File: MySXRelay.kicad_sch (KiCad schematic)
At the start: 52 parts, among them K1 FH44L-1AT-L1-DC5V, U1 MIC4427, U2 BL0942, U3 BP2525X, U4 Si8642BB-B-IS1, U5 MCP1703Ax-180xxTT, U8 AP2204K-ADJ, U9 ST485E

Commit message: update pcb (WIP)
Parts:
- removed C2: 1u, Capacitor_SMD:C_0603_1608Metric, symbol Device:C
- removed C3: 22u, Capacitor_SMD:C_1206_3216Metric, symbol Device:C
- removed D1, D2: BAT54S, Package_TO_SOT_SMD:SOT-23, symbol Diode:BAT54S
- removed K1: FH44L-1AT-L1-DC5V, MySXRelay:RELAY-TH_FH44L-1AT-L1-DC5V, symbol MySXRelay:Relay_SPST_Latching_1coil
- removed R1: 10k, Resistor_SMD:R_0603_1608Metric, symbol Device:R
- removed R21: 9.1k, Resistor_SMD:R_0603_1608Metric, symbol Device:R
- removed R23: 3k, Resistor_SMD:R_0603_1608Metric, symbol Device:R
- removed U1: MIC4427, Package_SO:SOIC-8_3.9x4.9mm_P1.27mm, symbol Driver_FET:MIC4427
- added J3: Relay, MySXRelay:edge_connector, symbol MySXRelay:edge_connector
- C1: value 100n -> 10u; footprint Capacitor_SMD:C_0402_1005Metric -> Capacitor_SMD:C_0603_1608Metric
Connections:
- net +5V: now also J3.4 (VCC); no longer C1.1
- net D5: now also J3.3 (REL)
- net GND: now also J3.5 (GND); no longer C1.2
- net GND1: now also C1.1
- net L_IN: now also J3.1 (A1)
- net L_OUT: now also J3.2 (A2)
- net at U8.4 (ADJ): now also C1.2
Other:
- moved on the sheet: C19

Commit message: update pcb (WIP)
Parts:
- C1: value 10u -> 100p; footprint Capacitor_SMD:C_0603_1608Metric -> Capacitor_SMD:C_0402_1005Metric
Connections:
- net BP2525_DRAIN: now reaches C5.1, D5.1 (K), U3.4 (DRAIN)
- net BP2525_CS: now reaches R7.2, U3.5 (CS)
- net L_SENSE: now reaches R17.1, R18.2
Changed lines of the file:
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@@
 	)
 	(junction
+		(at 162.56 67.31)
+		(diameter 0)
+		(color 0 0 0 0)
+	)
+	(junction
 		(at 96.52 119.38)
 		(diameter 0)
@@
 	(wire
 		(pts
+			(xy 166.37 63.5) (xy 162.56 63.5)
+		)
+		(stroke
+			(width 0)
+			(type default)
+		)
+	)
+	(wire
+		(pts
 			(xy 223.52 106.68) (xy 226.06 106.68)
 		)
@@
 	(wire
 		(pts
+			(xy 162.56 63.5) (xy 162.56 67.31)
+		)
+		(stroke
+			(width 0)
+			(type default)
+		)
+	)
+	(wire
+		(pts
 			(xy 87.63 160.02) (xy 68.58 160.02)
 		)
@@
 		)
 	)
+	(label "BP2525_CS"
+		(at 175.26 143.51 90)
+		(fields_autoplaced yes)
+		(effects
+			(font
+				(size 1.27 1.27)
+			)
+			(justify left bottom)
+		)
+	)
+	(label "BP2525_DRAIN"
+		(at 173.99 119.38 0)
+		(fields_autoplaced yes)
+		(effects
+			(font
+				(size 1.27 1.27)
+			)
+			(justify left bottom)
+		)
+	)
+	(global_label "L_SENSE"
+		(shape input)
+		(at 166.37 63.5 0)
+		(fields_autoplaced yes)
+		(effects
+			(font
+				(size 1.27 1.27)
+			)
+			(justify left)
+		)
+		(property "Intersheetrefs" "${INTERSHEET_REFS}"
+			(at 177.3984 63.5 0)
+			(effects
+				(font
+					(size 1.27 1.27)
+				)
+				(justify left)
+				(hide yes)
+			)
+		)
+	)
 	(global_label "RS485_TX"
 		(shape input)
@@
 		)
 		(property "Netclass" "Mains_HV"
-			(at 188.976 116.332 0)
+			(at 188.976 115.824 0)
 			(effects
 				(font
@@
 		(on_board yes)
 		(dnp no)
-		(fields_autoplaced yes)
 		(property "Reference" "#PWR032"
 			(at 162.56 64.77 0)
@@
 		)
 		(property "Value" "GND"
-			(at 162.56 63.5 0)
+			(at 159.258 60.706 0)
 			(effects
 				(font
@@
 			)
 		)
-		(property "Value" "10u"
+		(property "Value" "100p"
 			(at 92.71 114.3001 0)
 			(effects
@@
 			)
 		)
-		(property "Footprint" "Capacitor_SMD:C_0603_1608Metric"
+		(property "Footprint" "Capacitor_SMD:C_0402_1005Metric"
 			(at 95.5548 111.76 0)
 			(effects

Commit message: relay module updated
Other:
- moved on the sheet: J3
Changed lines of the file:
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@@
 	(wire
 		(pts
-			(xy 62.23 46.99) (xy 63.5 46.99)
+			(xy 44.45 55.88) (xy 45.72 55.88)
 		)
 		(stroke
@@
 	(wire
 		(pts
-			(xy 62.23 53.34) (xy 63.5 53.34)
+			(xy 44.45 62.23) (xy 45.72 62.23)
 		)
 		(stroke
@@
 	(wire
 		(pts
-			(xy 62.23 49.53) (xy 63.5 49.53)
+			(xy 44.45 58.42) (xy 45.72 58.42)
 		)
 		(stroke
@@
 	(wire
 		(pts
-			(xy 62.23 55.88) (xy 63.5 55.88)
+			(xy 44.45 64.77) (xy 45.72 64.77)
 		)
 		(stroke
@@
 	(wire
 		(pts
-			(xy 62.23 58.42) (xy 63.5 58.42)
+			(xy 44.45 67.31) (xy 45.72 67.31)
 		)
 		(stroke
@@
 	(global_label "L_IN"
 		(shape input)
-		(at 62.23 46.99 180)
+		(at 44.45 55.88 180)
 		(fields_autoplaced yes)
 		(effects
@@
 		)
 		(property "Intersheetrefs" "${INTERSHEET_REFS}"
-			(at 55.3138 46.99 0)
+			(at 37.5338 55.88 0)
 			(effects
 				(font
@@
 	(global_label "D5"
 		(shape input)
-		(at 62.23 53.34 180)
+		(at 44.45 62.23 180)
 		(fields_autoplaced yes)
 		(effects
@@
 		)
 		(property "Intersheetrefs" "${INTERSHEET_REFS}"
-			(at 56.7653 53.34 0)
+			(at 38.9853 62.23 0)
 			(effects
 				(font
@@
 	(global_label "L_OUT"
 		(shape input)
-		(at 62.23 49.53 180)
+		(at 44.45 58.42 180)
 		(fields_autoplaced yes)
 		(effects
@@
 		)
 		(property "Intersheetrefs" "${INTERSHEET_REFS}"
-			(at 53.6205 49.53 0)
+			(at 35.8405 58.42 0)
 			(effects
 				(font
@@
 	(symbol
 		(lib_id "MySXRelay:edge_connector")
-		(at 72.39 52.07 0)
+		(at 54.61 60.96 0)
 		(unit 1)
 		(exclude_from_sim no)
@@
 		(fields_autoplaced yes)
 		(property "Reference" "J3"
-			(at 78.74 50.7999 0)
+			(at 60.96 59.6899 0)
 			(effects
 				(font
@@
 		)
 		(property "Value" "Relay"
-			(at 78.74 53.3399 0)
+			(at 60.96 62.2299 0)
 			(effects
 				(font
@@
 		)
 		(property "Footprint" "MySXRelay:edge_connector"
-			(at 72.39 62.23 0)
+			(at 54.61 71.12 0)
 			(effects
 				(font
@@
 		)
 		(property "Datasheet" ""
-			(at 66.04 71.12 0)
+			(at 48.26 80.01 0)
 			(effects
 				(font
@@
 		)
 		(property "Description" "Relay board edge connector"
-			(at 72.39 52.07 0)
+			(at 54.61 60.96 0)
 			(effects
 				(font
@@
 	(symbol
 		(lib_id "power:+5V")
-		(at 62.23 55.88 90)
+		(at 44.45 64.77 90)
 		(unit 1)
 		(exclude_from_sim no)
@@
 		(fields_autoplaced yes)
 		(property "Reference" "#PWR03"
-			(at 66.04 55.88 0)
+			(at 48.26 64.77 0)
 			(effects
 				(font
@@
 		)
 		(property "Value" "+5V"
-			(at 58.42 55.8799 90)
+			(at 40.64 64.7699 90)
 			(effects
 				(font
@@
 		)
 		(property "Footprint" ""
-			(at 62.23 55.88 0)
+			(at 44.45 64.77 0)
 			(effects
 				(font
@@
 		)
 		(property "Datasheet" ""
-			(at 62.23 55.88 0)
+			(at 44.45 64.77 0)
 			(effects
 				(font
@@
 		)
 		(property "Description" "Power symbol creates a global label with name \"+5V\""
-			(at 62.23 55.88 0)
+			(at 44.45 64.77 0)
 			(effects
 				(font
@@
 		(lib_name "GND_1")
 		(lib_id "power:GND")
-		(at 62.23 58.42 270)
+		(at 44.45 67.31 270)
 		(unit 1)
 		(exclude_from_sim no)
@@
 		(fields_autoplaced yes)
 		(property "Reference" "#PWR040"
-			(at 55.88 58.42 0)
+			(at 38.1 67.31 0)
 			(effects
 				(font
@@
 		)
 		(property "Value" "GND"
-			(at 58.42 58.4199 90)
+			(at 40.64 67.3099 90)
 			(effects
 				(font
@@
 		)
 		(property "Footprint" ""
-			(at 62.23 58.42 0)
+			(at 44.45 67.31 0)
 			(effects
 				(font
@@
 		)
 		(property "Datasheet" ""
-			(at 62.23 58.42 0)
+			(at 44.45 67.31 0)
 			(effects
 				(font
@@
 		)
 		(property "Description" "Power symbol creates a global label with name \"GND\" , ground"
-			(at 62.23 58.42 0)
+			(at 44.45 67.31 0)
 			(effects
 				(font
@@
 	)
 	(sheet
-		(at 217.424 22.606)
-		(size 44.196 66.802)
+		(at 82.55 38.1)
+		(size 26.162 32.258)
 		(fields_autoplaced yes)
 		(stroke
@@
 		)
 		(property "Sheetname" "MCU"
-			(at 217.424 21.8944 0)
+			(at 82.55 37.3884 0)
 			(effects
 				(font
@@
 		)
 		(property "Sheetfile" "mcu.kicad_sch"
-			(at 217.424 89.9926 0)
+			(at 82.55 70.9426 0)
 			(effects
 				(font

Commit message: changed mains connector
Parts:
- X2: footprint MySXRelay:MSTB_2,5_4-G -> TerminalBlock_Phoenix:TerminalBlock_Phoenix_MKDS-1,5-4-5.08_1x04_P5.08mm_Horizontal
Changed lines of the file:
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@@
 			)
 		)
-		(property "Footprint" "MySXRelay:MSTB_2,5_4-G"
+		(property "Footprint" "TerminalBlock_Phoenix:TerminalBlock_Phoenix_MKDS-1,5-4-5.08_1x04_P5.08mm_Horizontal"
 			(at 231.14 104.14 0)
 			(effects

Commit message: change AP2204 to AP2202
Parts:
- U8: value AP2204K-ADJ -> AP2202K-5.0
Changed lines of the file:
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@@
 			)
 		)
-		(property "Value" "AP2204K-ADJ"
+		(property "Value" "AP2202K-5.0"
 			(at 105.41 105.41 0)
 			(effects
@@
 			)
 		)
-		(property "Datasheet" "https://www.diodes.com/assets/Datasheets/products_inactive_data/AP2204.pdf"
+		(property "Datasheet" "https://www.diodes.com/assets/Datasheets/AP2202.pdf"
 			(at 105.41 109.22 0)
 			(effects

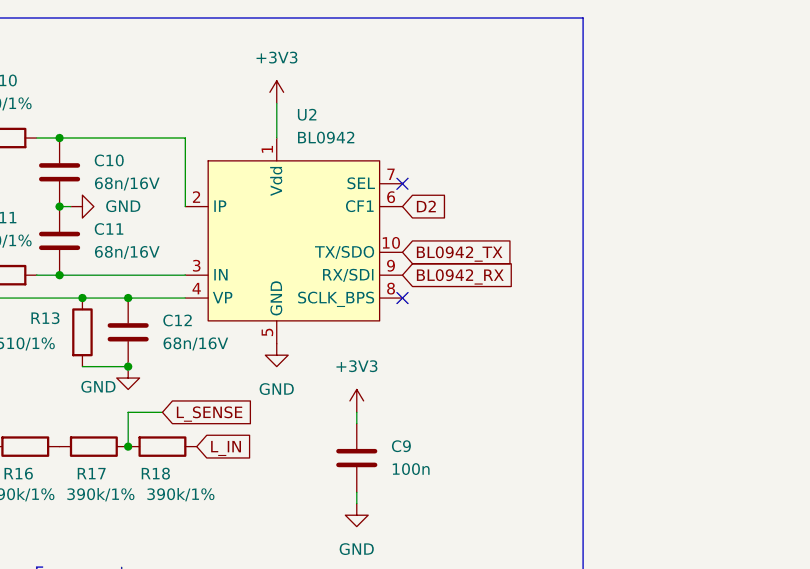
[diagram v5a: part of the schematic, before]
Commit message: remove BL0942 TX pin jumper and add pull up resistor
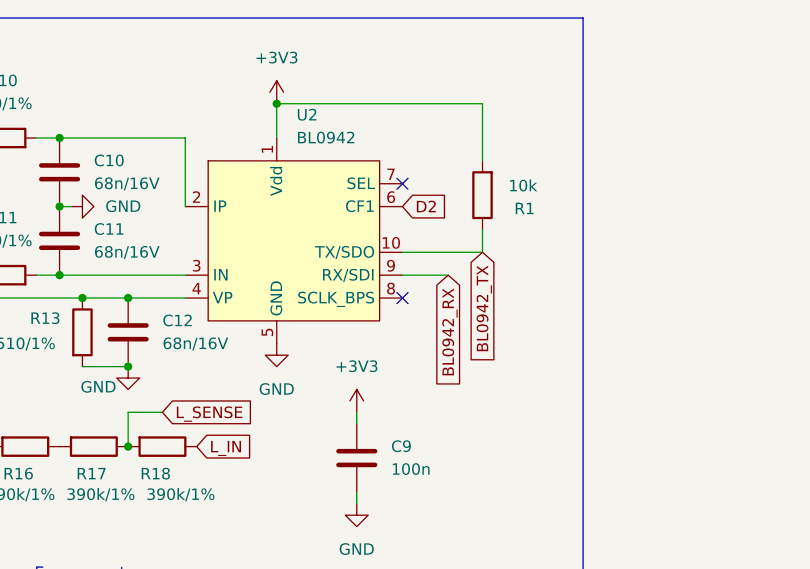
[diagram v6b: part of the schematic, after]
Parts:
- added R1: 10k, Resistor_SMD:R_0603_1608Metric, symbol Device:R
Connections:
- net +3V3: now also R1.2
- net BL0942_TX: now also R1.1
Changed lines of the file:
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@@
 	)
 	(junction
+		(at 179.07 29.21)
+		(diameter 0)
+		(color 0 0 0 0)
+	)
+	(junction
 		(at 110.49 119.38)
 		(diameter 0)
@@
 	(wire
 		(pts
+			(xy 201.93 45.72) (xy 193.04 45.72)
+		)
+		(stroke
+			(width 0)
+			(type default)
+		)
+	)
+	(wire
+		(pts
 			(xy 237.49 151.13) (xy 247.65 151.13)
 		)
@@
 	(wire
 		(pts
+			(xy 201.93 29.21) (xy 179.07 29.21)
+		)
+		(stroke
+			(width 0)
+			(type default)
+		)
+	)
+	(wire
+		(pts
 			(xy 44.45 162.56) (xy 45.72 162.56)
 		)
@@
 	(wire
 		(pts
+			(xy 201.93 43.18) (xy 201.93 45.72)
+		)
+		(stroke
+			(width 0)
+			(type default)
+		)
+	)
+	(wire
+		(pts
 			(xy 45.72 134.62) (xy 45.72 142.24)
 		)
@@
 	(wire
 		(pts
+			(xy 201.93 35.56) (xy 201.93 29.21)
+		)
+		(stroke
+			(width 0)
+			(type default)
+		)
+	)
+	(wire
+		(pts
 			(xy 135.89 109.22) (xy 135.89 149.86)
 		)
@@
 	(wire
 		(pts
+			(xy 198.12 48.26) (xy 193.04 48.26)
+		)
+		(stroke
+			(width 0)
+			(type default)
+		)
+	)
+	(wire
+		(pts
 			(xy 199.39 119.38) (xy 173.99 119.38)
 		)
@@
 	(global_label "BL0942_RX"
 		(shape input)
-		(at 193.04 48.26 0)
+		(at 198.12 48.26 270)
 		(fields_autoplaced yes)
 		(effects
@@
 				(size 1.27 1.27)
 			)
-			(justify left)
+			(justify right)
 		)
 		(property "Intersheetrefs" "${INTERSHEET_REFS}"
-			(at 206.6084 48.26 0)
+			(at 198.12 61.8284 90)
 			(effects
 				(font
 					(size 1.27 1.27)
 				)
-				(justify left)
+				(justify right)
 				(hide yes)
 			)
@@
 	(global_label "BL0942_TX"
 		(shape input)
-		(at 193.04 45.72 0)
+		(at 201.93 45.72 270)
 		(fields_autoplaced yes)
 		(effects
@@
 				(size 1.27 1.27)
 			)
-			(justify left)
+			(justify right)
 		)
 		(property "Intersheetrefs" "${INTERSHEET_REFS}"
-			(at 206.306 45.72 0)
+			(at 201.93 58.986 90)
 			(effects
 				(font
 					(size 1.27 1.27)
 				)
-				(justify left)
+				(justify right)
 				(hide yes)
 			)
@@
 					(unit 1)
 				)
+			)
+		)
+	)
+	(symbol
+		(lib_id "Device:R")
+		(at 201.93 39.37 180)
+		(unit 1)
+		(exclude_from_sim no)
+		(in_bom yes)
+		(on_board yes)
+		(dnp no)
+		(property "Reference" "R1"
+			(at 207.772 40.894 0)
+			(effects
+				(font
+					(size 1.27 1.27)
+				)
+				(justify left)
+			)
+		)
+		(property "Value" "10k"
+			(at 208.026 38.354 0)
+			(effects
+				(font
+					(size 1.27 1.27)
+				)
+				(justify left)
+			)
+		)
+		(property "Footprint" "Resistor_SMD:R_0603_1608Metric"
+			(at 203.708 39.37 90)
+			(effects
+				(font
+					(size 1.27 1.27)
+				)
+				(hide yes)
+			)
+		)
+		(property "Datasheet" "~"
+			(at 201.93 39.37 0)
+			(effects
+				(font
+					(size 1.27 1.27)
+				)
+				(hide yes)
+			)
+		)
+		(property "Description" ""
+			(at 201.93 39.37 0)
+			(effects
+				(font
+					(size 1.27 1.27)
+				)
+				(hide yes)
+			)
+		)
+		(pin "1"
+		)
+		(pin "2"
+		)
+		(instances
+			(project "MySXRelay"
+				(path "/73ae532b-17b2-4152-9abe-0d6b33529f07"
+					(reference "R1")
+					(unit 1)
+				)

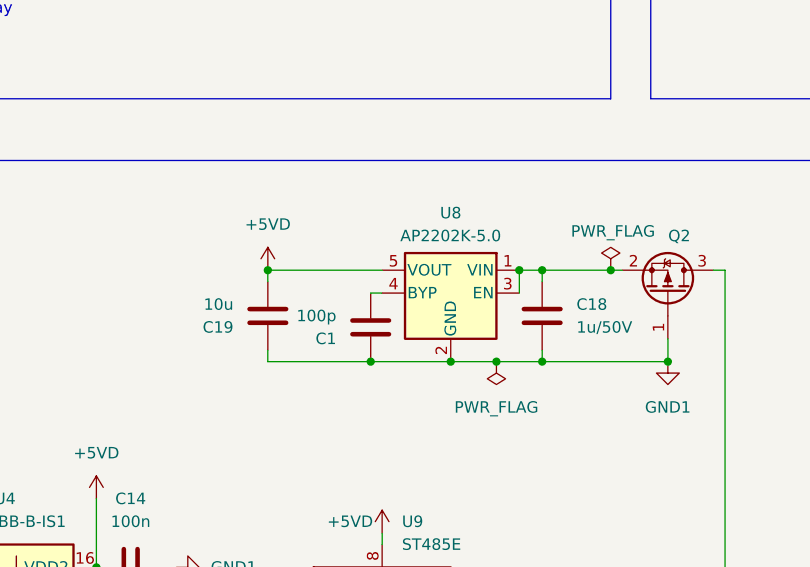
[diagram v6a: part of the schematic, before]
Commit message: change RS485 interface LDO package to sot-89
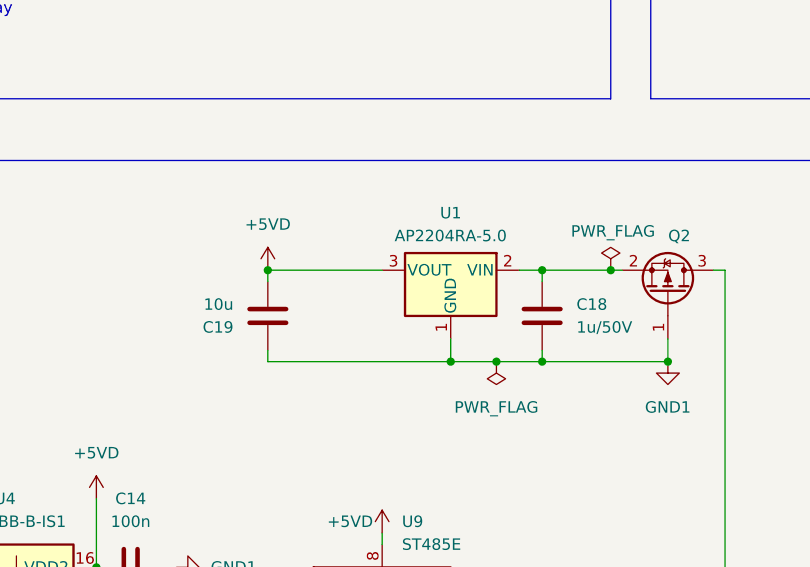
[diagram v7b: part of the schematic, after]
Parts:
- removed C1: 100p, Capacitor_SMD:C_0402_1005Metric, symbol Device:C
- removed U8: AP2202K-5.0, Package_TO_SOT_SMD:SOT-23-5, symbol Regulator_Linear:AP2204K-ADJ
- added U1: AP2204RA-5.0, Package_TO_SOT_SMD:SOT-89-3, symbol Regulator_Linear:AP2204RA-5.0
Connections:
- net +5VD: now also U1.3 (VOUT)
- net GND1: now also U1.1 (GND)
- net at C18.1, Q2.2 (S): now also U1.2 (VIN)
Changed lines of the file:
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@@
 	(paper "A4")
 	(junction
-		(at 105.41 119.38)
-		(diameter 0)
-		(color 0 0 0 0)
-	)
-	(junction
 		(at 237.49 151.13)
 		(diameter 0)
@@
 	)
 	(junction
+		(at 105.41 119.38)
+		(diameter 0)
+		(color 0 0 0 0)
+	)
+	(junction
 		(at 219.71 151.13)
 		(diameter 0)
@@
 	)
 	(junction
-		(at 113.03 109.22)
-		(diameter 0)
-		(color 0 0 0 0)
-	)
-	(junction
 		(at 123.19 152.4)
 		(diameter 0)
@@
 	)
 	(junction
-		(at 96.52 119.38)
-		(diameter 0)
-		(color 0 0 0 0)
-	)
-	(junction
 		(at 201.93 143.51)
 		(diameter 0)
@@
 	(wire
 		(pts
+			(xy 105.41 119.38) (xy 110.49 119.38)
+		)
+		(stroke
+			(width 0)
+			(type default)
+		)
+	)
+	(wire
+		(pts
 			(xy 224.79 151.13) (xy 224.79 146.05)
 		)
@@
 	(wire
 		(pts
+			(xy 105.41 116.84) (xy 105.41 119.38)
+		)
+		(stroke
+			(width 0)
+			(type default)
+		)
+	)
+	(wire
+		(pts
 			(xy 237.49 151.13) (xy 247.65 151.13)
 		)
@@
 	(wire
 		(pts
-			(xy 85.09 119.38) (xy 96.52 119.38)
+			(xy 85.09 119.38) (xy 105.41 119.38)
 		)
 		(stroke
@@
 	(wire
 		(pts
-			(xy 96.52 119.38) (xy 105.41 119.38)
-		)
-		(stroke
-			(width 0)
-			(type default)
-		)
-	)
-	(wire
-		(pts
 			(xy 144.78 33.02) (xy 143.51 33.02)
 		)
@@
 	(wire
 		(pts
-			(xy 113.03 109.22) (xy 115.57 109.22)
-		)
-		(stroke
-			(width 0)
-			(type default)
-		)
-	)
-	(wire
-		(pts
-			(xy 105.41 119.38) (xy 110.49 119.38)
-		)
-		(stroke
-			(width 0)
-			(type default)
-		)
-	)
-	(wire
-		(pts
 			(xy 110.49 119.38) (xy 115.57 119.38)
 		)
@@
 	(wire
 		(pts
-			(xy 113.03 109.22) (xy 113.03 111.76)
-		)
-		(stroke
-			(width 0)
-			(type default)
-		)
-	)
-	(wire
-		(pts
 			(xy 165.1 151.13) (xy 201.93 151.13)
 		)
@@
 	(wire
 		(pts
-			(xy 96.52 111.76) (xy 97.79 111.76)
+			(xy 214.63 138.43) (xy 219.71 138.43)
 		)
 		(stroke
@@
 	(wire
 		(pts
-			(xy 214.63 138.43) (xy 219.71 138.43)
+			(xy 201.93 35.56) (xy 201.93 29.21)
 		)
 		(stroke
@@
 	(wire
 		(pts
-			(xy 201.93 35.56) (xy 201.93 29.21)
+			(xy 135.89 109.22) (xy 135.89 149.86)
 		)
 		(stroke
@@
 	(wire
 		(pts
-			(xy 135.89 109.22) (xy 135.89 149.86)
+			(xy 198.12 48.26) (xy 193.04 48.26)
 		)
 		(stroke
@@
 	(wire
 		(pts
-			(xy 198.12 48.26) (xy 193.04 48.26)
+			(xy 199.39 119.38) (xy 173.99 119.38)
 		)
 		(stroke
@@
 	(wire
 		(pts
-			(xy 199.39 119.38) (xy 173.99 119.38)
+			(xy 115.57 109.22) (xy 113.03 109.22)
 		)
 		(stroke
@@
 		(length 2.54)
 		(shape round)
-		(at 113.03 109.22 0)
+		(at 115.57 109.22 0)
 		(effects
 			(font
@@
 		)
 		(property "Netclass" "EXT_VCC"
-			(at 115.062 108.458 90)
+			(at 117.602 108.458 90)
 			(effects
 				(font
@@
 		(length 2.54)
 		(shape round)
-		(at 96.52 111.76 90)
-		(effects
-			(font
-				(size 1.27 1.27)
-			)
-			(justify left bottom)
-		)
-		(property "Netclass" "EXT"
-			(at 89.662 111.76 0)
-			(effects
-				(font
-					(size 1.27 1.27)
-					(italic yes)
-				)
-				(justify left)
-			)
-		)
-	)
-	(netclass_flag ""
-		(length 2.54)
-		(shape round)
 		(at 185.42 111.76 180)
 		(effects
@@
 	)
 	(symbol
-		(lib_id "Device:C")
-		(at 96.52 115.57 180)
-		(unit 1)
-		(exclude_from_sim no)
-		(in_bom yes)
-		(on_board yes)
-		(dnp no)
-		(property "Reference" "C1"
-			(at 92.71 116.8401 0)
-			(effects
-				(font
-					(size 1.27 1.27)
-				)
-				(justify left)
-			)
-		)
-		(property "Value" "100p"
-			(at 92.71 114.3001 0)
-			(effects
-				(font
-					(size 1.27 1.27)
-				)
-				(justify left)
-			)
-		)
-		(property "Footprint" "Capacitor_SMD:C_0402_1005Metric"
-			(at 95.5548 111.76 0)
-			(effects
-				(font
-					(size 1.27 1.27)
-				)
-				(hide yes)
-			)
-		)
-		(property "Datasheet" "~"
-			(at 96.52 115.57 0)
-			(effects
-				(font
-					(size 1.27 1.27)
-				)
-				(hide yes)
-			)
-		)
-		(property "Description" ""
-			(at 96.52 115.57 0)
-			(effects
-				(font
-					(size 1.27 1.27)
-				)
-				(hide yes)
-			)
-		)
-		(pin "1"
-		)
-		(pin "2"
-		)
-		(instances
-			(project "MySXRelay"
-				(path "/73ae532b-17b2-4152-9abe-0d6b33529f07"
-					(reference "C1")
-					(unit 1)
-				)
-			)
-		)
-	)
-	(symbol
 		(lib_id "Diode:SMAJ11CA")
 		(at 123.19 162.56 90)
@@
 	)
 	(symbol
-		(lib_id "Regulator_Linear:AP2204K-ADJ")
-		(at 105.41 111.76 0)
-		(mirror y)
-		(unit 1)
-		(exclude_from_sim no)
-		(in_bom yes)
-		(on_board yes)
-		(dnp no)
-		(property "Reference" "U8"
-			(at 105.41 102.87 0)
-			(effects
-				(font
-					(size 1.27 1.27)
-				)
-			)
-		)
-		(property "Value" "AP2202K-5.0"
-			(at 105.41 105.41 0)
-			(effects
-				(font
-					(size 1.27 1.27)
-				)
-			)
-		)
-		(property "Footprint" "Package_TO_SOT_SMD:SOT-23-5"
-			(at 105.41 103.505 0)
-			(effects
-				(font
-					(size 1.27 1.27)
-				)
-				(hide yes)
-			)
-		)
-		(property "Datasheet" "https://www.diodes.com/assets/Datasheets/AP2202.pdf"
-			(at 105.41 109.22 0)
-			(effects
-				(font
-					(size 1.27 1.27)
-				)
-				(hide yes)
-			)
-		)
-		(property "Description" "150mA low dropout adjustable linear regulator, wide input voltage range, SOT-23-5 package"
-			(at 105.41 111.76 0)
-			(effects
-				(font
-					(size 1.27 1.27)
-				)
-				(hide yes)
-			)
-		)
-		(pin "2"
-		)
-		(pin "5"
-		)
-		(pin "3"
-		)
-		(pin "1"
-		)
-		(pin "4"
-		)
-		(instances
-			(project ""
-				(path "/73ae532b-17b2-4152-9abe-0d6b33529f07"
-					(reference "U8")
-					(unit 1)
-				)
-			)
-		)
-	)
-	(symbol
 		(lib_id "Connector_Generic:Conn_01x04")
 		(at 140.97 152.4 0)
@@
 					(unit 1)
 				)
+			)
+		)
+	)
+	(symbol
+		(lib_id "Regulator_Linear:AP2204RA-5.0")
+		(at 105.41 109.22 0)
+		(mirror y)
+		(unit 1)
+		(exclude_from_sim no)
+		(in_bom yes)
+		(on_board yes)
+		(dnp no)
+		(property "Reference" "U1"
+			(at 105.41 102.87 0)
+			(effects
+				(font
+					(size 1.27 1.27)
+				)
+			)
+		)
+		(property "Value" "AP2204RA-5.0"
+			(at 105.41 105.41 0)
+			(effects
+				(font
+					(size 1.27 1.27)
+				)
+			)
+		)
+		(property "Footprint" "Package_TO_SOT_SMD:SOT-89-3"
+			(at 105.41 103.505 0)
+			(effects
+				(font
+					(size 1.27 1.27)
+				)
+				(hide yes)
+			)
+		)
+		(property "Datasheet" "https://www.diodes.com/assets/Datasheets/products_inactive_data/AP2204.pdf"
+			(at 105.41 109.22 0)
+			(effects
+				(font
+					(size 1.27 1.27)
+				)
+				(hide yes)
+			)
+		)
+		(property "Description" "150mA low dropout linear regulator, wide input voltage range, 5.0V fixed positive output, SOT-89-3 package"
+			(at 105.41 109.22 0)
+			(effects
+				(font
+					(size 1.27 1.27)
+				)
+				(hide yes)
+			)
+		)
+		(pin "1"
+		)
+		(pin "3"
+		)
+		(pin "2"
+		)
+		(instances
+			(project ""
+				(path "/73ae532b-17b2-4152-9abe-0d6b33529f07"
+					(reference "U1")
+					(unit 1)
+				)
